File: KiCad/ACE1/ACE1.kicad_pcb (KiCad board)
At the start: 2 copper layers, 198.1 x 200.7 mm, 147 parts, among them IC1 78T, Q1 2N3904, Q2 2N2369, Q3 BC183, Q4 2N3904, X1 6.556MHz

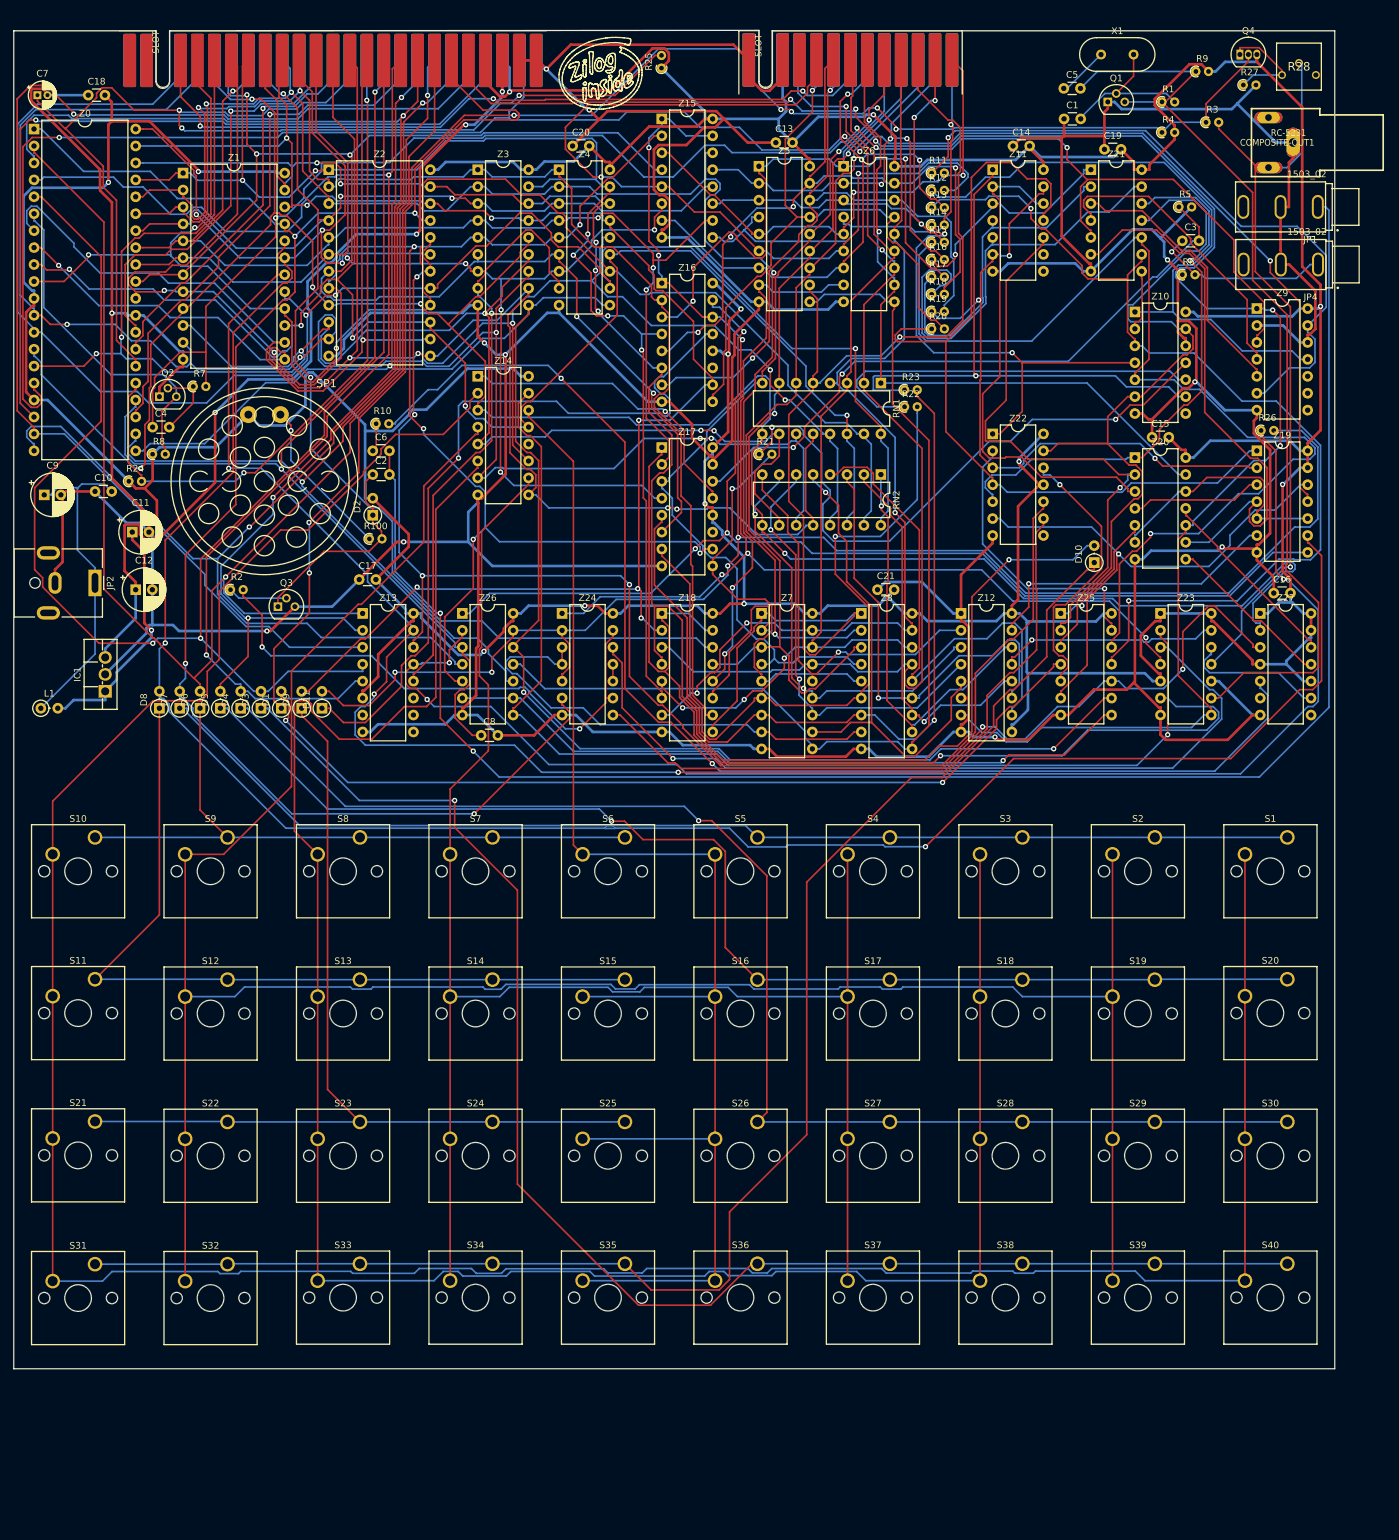
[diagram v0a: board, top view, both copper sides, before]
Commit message: Renumber components to match original Schema.
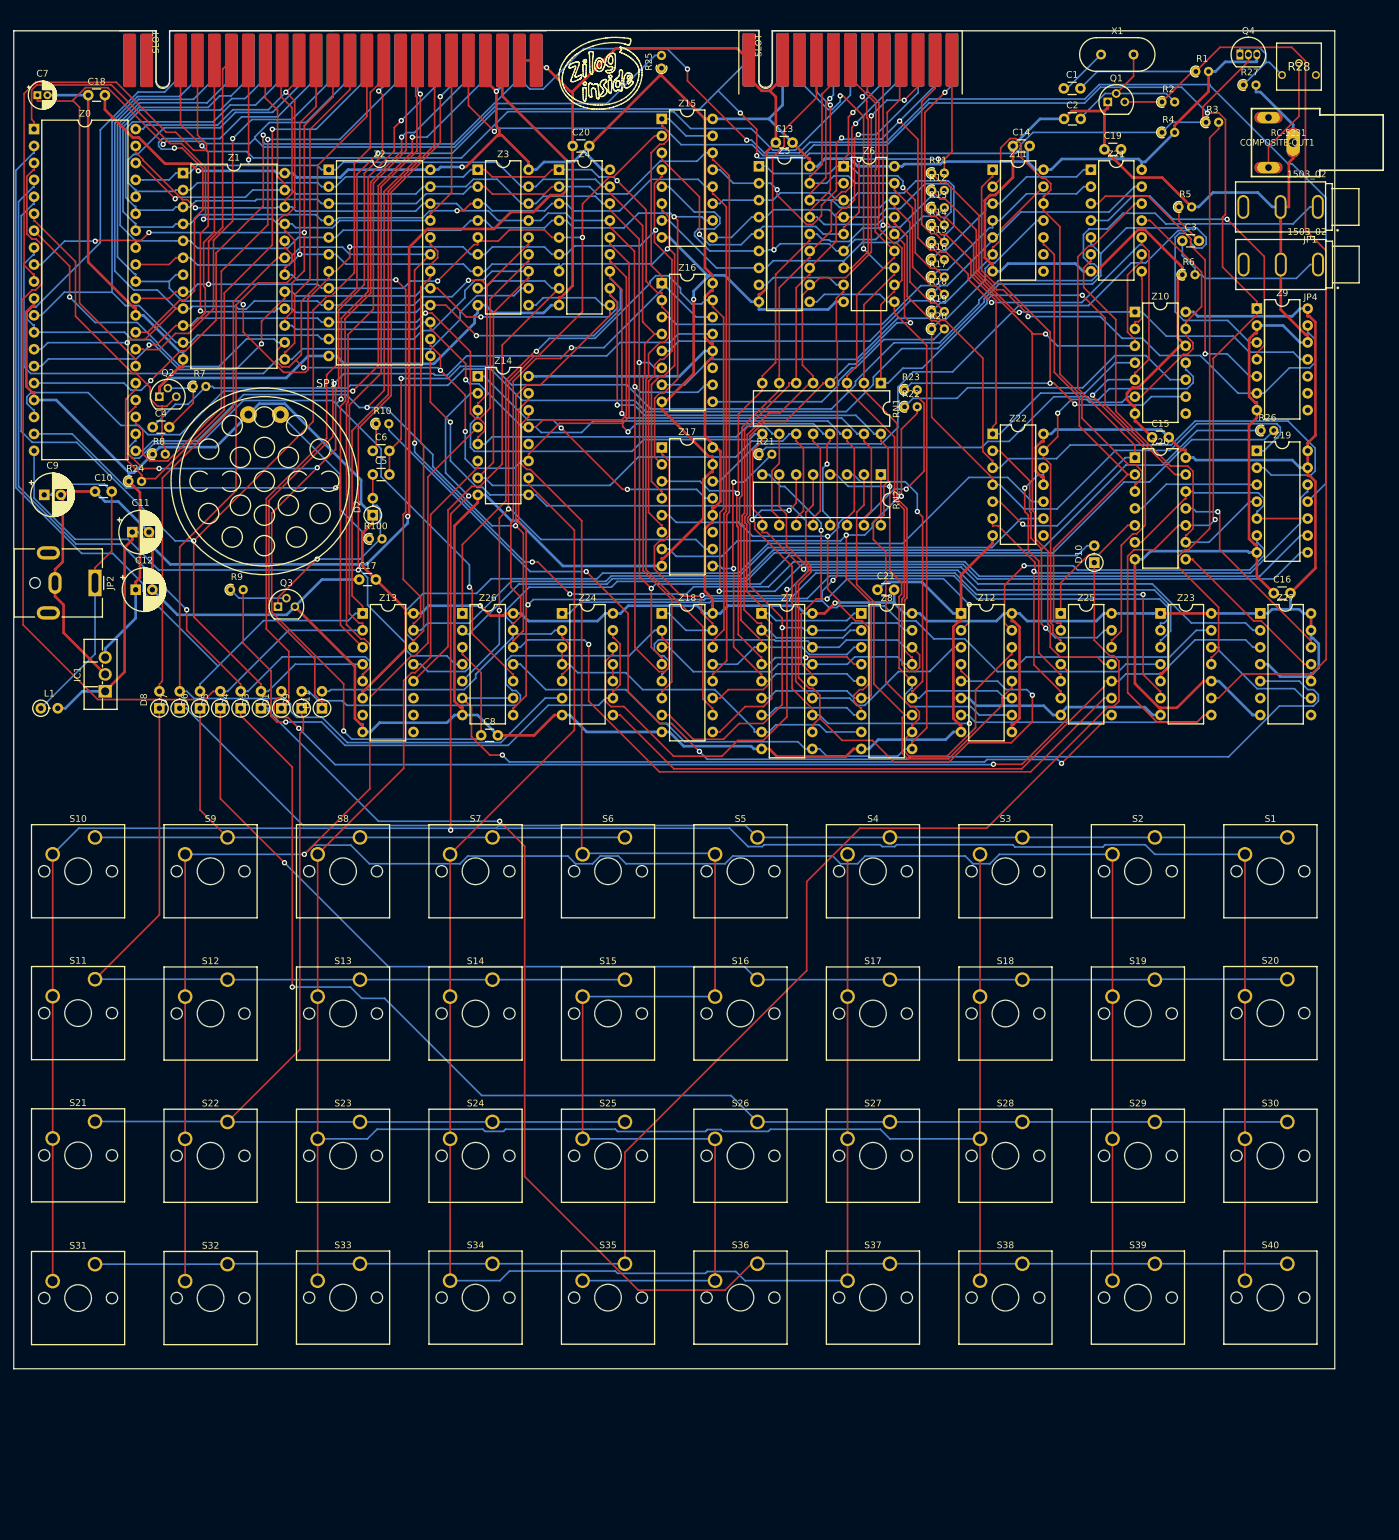
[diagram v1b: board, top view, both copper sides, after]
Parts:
- C1: renamed from C5; value 47N -> 30p
- C2: renamed from C1; value 47N -> 100
- C5: renamed from C2; value 47N -> 47p
- R1: renamed from R9; value 47k -> 4k7
- R9: renamed from R2; value 12k -> 22k
- renumbered R1 to R2
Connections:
- C5 pad 1: Net-(C2-Pad1) -> Net-(C5-Pad1)
- D2 pad 1: Net-(C2-Pad1) -> VCC
- D2 pad 2: VCC -> Net-(C5-Pad1)
- Q3 pad 1: Net-(C2-Pad1) -> Net-(C5-Pad1)
- R100 pad 2: Net-(C2-Pad1) -> Net-(C5-Pad1)
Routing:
- net VCC: track 958.2 -> 820.0 mm, vias 13 -> 5
- net Net-(C5-Pad2): track 261.3 -> 177.4 mm, vias 2 -> 1
- net GND: track 1071.6 -> 999.0 mm, vias 11 -> 2
- net Net-(R26-Pad1): track 206.1 -> 147.2 mm, vias 3 -> 0
- net /AD10: track 386.5 -> 332.6 mm, vias 5 -> 4
- net Net-(Z1-Pad18): track 232.5 -> 179.5 mm, vias 3 -> 1
- net /AD8: track 291.0 -> 243.5 mm, vias 6 -> 3
- net /CNT7: track 159.3 -> 114.1 mm, vias 1 -> 2
- net /~MREQ: track 190.8 -> 147.4 mm, vias 1 -> 2
- net /DA0: track 347.1 -> 305.9 mm, vias 5 -> 3
- net /H1A1: track 131.4 -> 90.7 mm, vias 2 -> 1
- net /DA1: track 258.4 -> 219.3 mm, vias 6 -> 2
- net /~VHOLD: track 176.9 -> 214.9 mm, vias 3 -> 2
- net /AD0: track 273.4 -> 236.7 mm, vias 7 -> 5
- net Net-(Z13-Pad14): track 211.6 -> 175.4 mm, vias 4 -> 0
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
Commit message: Double check transistors
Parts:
- renumbered Z18 to Z17, Z17 to Z18, Z12 to Z28, Z13 to Z29
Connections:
- E1 pad CLK: /~CLK -> /PHI
- Q2 pad 3: Net-(Q2-Pad3) -> /PHI
- R8 pad 2: Net-(Q2-Pad3) -> /PHI
- Z0 pad 6: Net-(Q2-Pad3) -> /PHI
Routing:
- net GND: track 999.0 -> 0.00 mm, vias 2 -> 0
- net VCC: track 820.0 -> 0.00 mm, vias 5 -> 0
- net Net-(S1-Pad2): track 381.8 -> 0.00 mm, vias 2 -> 0
- net Net-(S12-Pad2): track 348.3 -> 0.00 mm, vias 1 -> 0
- net /AD10: track 332.6 -> 0.00 mm, vias 4 -> 0
- net /DA0: track 305.9 -> 0.00 mm, vias 3 -> 0
- net /~WR: track 305.8 -> 0.00 mm, vias 4 -> 0
- net /~INT: track 298.9 -> 0.00 mm, vias 4 -> 0
- net Net-(S13-Pad2): track 298.5 -> 0.00 mm
- net Net-(D11-Pad2): track 292.8 -> 0.00 mm, vias 1 -> 0
- net /~CLK: track 284.4 -> 0.00 mm, vias 3 -> 0
- net /AD9: track 259.1 -> 0.00 mm, vias 2 -> 0
- net Net-(S14-Pad2): track 256.0 -> 0.00 mm
- net /DA4: track 254.4 -> 0.00 mm, vias 6 -> 0
- net /AD11: track 250.1 -> 0.00 mm, vias 1 -> 0
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
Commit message: Added routing.
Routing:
- net GND: track 0.00 -> 994.0 mm, vias 0 -> 1
- net VCC: track 0.00 -> 836.2 mm, vias 0 -> 4
- net Net-(S1-Pad2): track 0.00 -> 384.5 mm, vias 0 -> 1
- net /AD10: track 0.00 -> 343.0 mm, vias 0 -> 1
- net Net-(S12-Pad2): track 0.00 -> 341.9 mm, vias 0 -> 1
- net /DA0: track 0.00 -> 325.4 mm, vias 0 -> 4
- net /~INT: track 0.00 -> 314.8 mm, vias 0 -> 1
- net Net-(D11-Pad2): track 0.00 -> 302.9 mm
- net Net-(S13-Pad2): track 0.00 -> 299.2 mm
- net /~WR: track 0.00 -> 284.7 mm, vias 0 -> 4
- net /VIDEO: track 0.00 -> 278.6 mm, vias 0 -> 3
- net Net-(D10-Pad1): track 0.00 -> 275.9 mm, vias 0 -> 1
- net /AD11: track 0.00 -> 271.8 mm, vias 0 -> 1
- net /AD9: track 0.00 -> 259.4 mm, vias 0 -> 1
- net Net-(S14-Pad2): track 0.00 -> 259.3 mm
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
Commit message: Add space key. Re-jig PCB positions.
Signed-off-by: John Bradley <flypie@rocketmail.com>
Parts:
- moved S40 92.2 mm to (177.8, 248.9)
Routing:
- net Net-(S1-Pad2): track 384.5 -> 460.5 mm
- net Net-(D3-Pad1): track 200.7 -> 207.4 mm
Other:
- board size 198.1 x 200.7 mm -> 198.2 x 224.4 mm

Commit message: ACE2NOKBV2MK2 update IC placement. Reverse Diode.
Signed-off-by: John Bradley <flypie@rocketmail.com>
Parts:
- added KEYBOARD1: Conn_02x08_Odd_Even, Connector_PinHeader_2.54mm:PinHeader_2x08_P2.54mm_Vertical, F.Cu at (101.6, 153.7)
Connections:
- net Net-(D10-Pad1) renamed /ROW8
- net Net-(D3-Pad1) renamed /ROW15
- net Net-(D4-Pad1) renamed /ROW14
- net Net-(D5-Pad1) renamed /ROW13
- net Net-(D6-Pad1) renamed /ROW12
- net Net-(D7-Pad1) renamed /ROW11
- net Net-(D8-Pad1) renamed /ROW10
- net Net-(D9-Pad1) renamed /ROW9
- net Net-(S1-Pad2) renamed /COLA
- net Net-(S12-Pad2) renamed /COLB
- net Net-(S13-Pad2) renamed /COLC
- net Net-(S14-Pad2) renamed /COLD
- net Net-(S15-Pad2) renamed /COLE
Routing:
- net /ROW8: track 275.9 -> 373.3 mm, vias 1 -> 5
- net /COLE: track 220.9 -> 267.2 mm, vias 0 -> 1
- net /ROW9: track 146.1 -> 179.0 mm
- net /COLD: track 259.3 -> 291.2 mm, vias 0 -> 2
- net /COLC: track 299.2 -> 327.2 mm
- net /ROW11: track 174.6 -> 190.8 mm
- net /COLB: track 341.9 -> 356.2 mm
- net /COLA: track 460.5 -> 472.9 mm
- net /ROW13: track 181.8 -> 185.5 mm
- net /ROW12: track 100.7 -> 104.2 mm
- net /ROW10: track 124.1 -> 127.1 mm
- net /ROW14: track 184.3 -> 186.6 mm
- net /ROW15: track 207.4 -> 209.3 mm
